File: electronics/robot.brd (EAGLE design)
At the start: 170.3 x 155.9 mm, 83 parts, among them J1 USB-B, J3 B6B-ZR, J4 B6B-ZR, J5 B6B-ZR, J6 KICKER, Q1 IRLMS2002TRPBF, Q2 IRLMS2002TRPBF, Q3 NPN_BC817,215, Q4 SUD50N04-8M8P-4GE3, Q5 NPN_BC817,215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

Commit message: Electronic fixes
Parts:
- removed S1: DPDT, rhoban:L202021MA04Q
- added C17: 1µF, SparkFun-Capacitors:0805
- added Q7: IRLMS2002TRPBF, rhoban:SOT23-6
- added R18: 56K, SparkFun-Resistors:0805
- added U$1: L102011ML04Q, rhoban:L102011ML04Q
- moved J2 24.0 mm to (30.5, 7.39)
- moved Q1 8.75 mm to (22.4, 23.6)
- moved Q2 8.75 mm to (18.7, 23.6)
- moved R3 8.75 mm to (20.7, 17.1)
- moved R5 8.75 mm to (17.0, 17.1)
- moved U3 8.75 mm to (26.1, 23.6)
- moved C7 8.75 mm to (21.1, 27.9)
- moved C8 8.75 mm to (23.4, 27.8)
- moved R10 8.75 mm to (15.6, 23.7)
- moved R11 8.75 mm to (24.4, 20.1)
- moved R7 8.75 mm to (25.9, 27.8)
- moved R9 8.75 mm to (17.7, 28.9)
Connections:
- new net N$19: C17.2, Q7.3, R18.2
- net GND_RAW: now also Q7.4, R18.1; no longer S1.P4
- net N$13: now also Q7.1, Q7.2, Q7.5, Q7.6; no longer S1.P5
- net N$7: now also U$1.P$2; no longer S1.P2
- net VIN: now also C17.1, U$1.P$1; no longer S1.P3

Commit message: Upgrading capacitors to 3300uF
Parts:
- C19, C20: value 2200uF -> 3300uF
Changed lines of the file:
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@@
 <attribute name="FARNELL" value="JF-0530B" x="-63.639453125" y="27.664428125" size="1.778" layer="27" font="vector" rot="R330" display="off"/>
 </element>
-<element name="C19" library="rcl" package="E5-13" value="2200uF" x="-46.560271875" y="45.22785625" rot="R240">
-<attribute name="FARNELL" value="2749341" x="-46.560271875" y="45.22785625" size="1.778" layer="27" rot="R240" display="off"/>
+<element name="C19" library="rcl" package="E5-13" value="3300uF" x="-46.560271875" y="45.22785625" rot="R240">
+<attribute name="MOUSER" value="710-860160278042 " x="-46.560271875" y="45.22785625" size="1.778" layer="27" rot="R240" display="off"/>
 </element>
-<element name="C20" library="rcl" package="E5-13" value="2200uF" x="-63.309496875" y="17.42513125" rot="R60">
-<attribute name="FARNELL" value="2749341" x="-63.309496875" y="17.42513125" size="1.778" layer="27" rot="R60" display="off"/>
+<element name="C20" library="rcl" package="E5-13" value="3300uF" x="-63.309496875" y="17.42513125" rot="R60">
+<attribute name="MOUSER" value="710-860160278042 " x="-63.309496875" y="17.42513125" size="1.778" layer="27" rot="R60" display="off"/>
 </element>
 <element name="C1" library="SparkFun-Capacitors" package="0805" value="0.1µF" x="-19.29488125" y="-38.44696875" rot="R300">

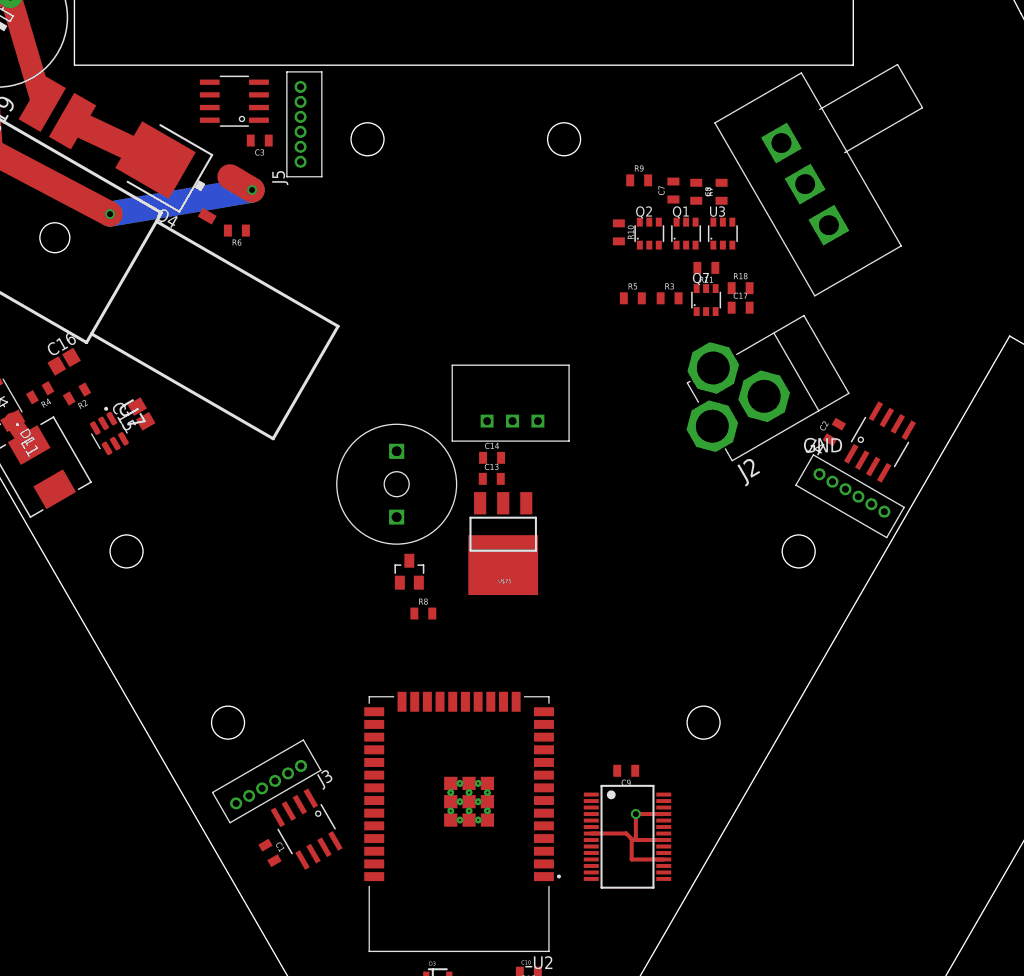
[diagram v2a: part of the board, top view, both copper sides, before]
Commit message: Preparing a switch to TOSHIBA H bridges
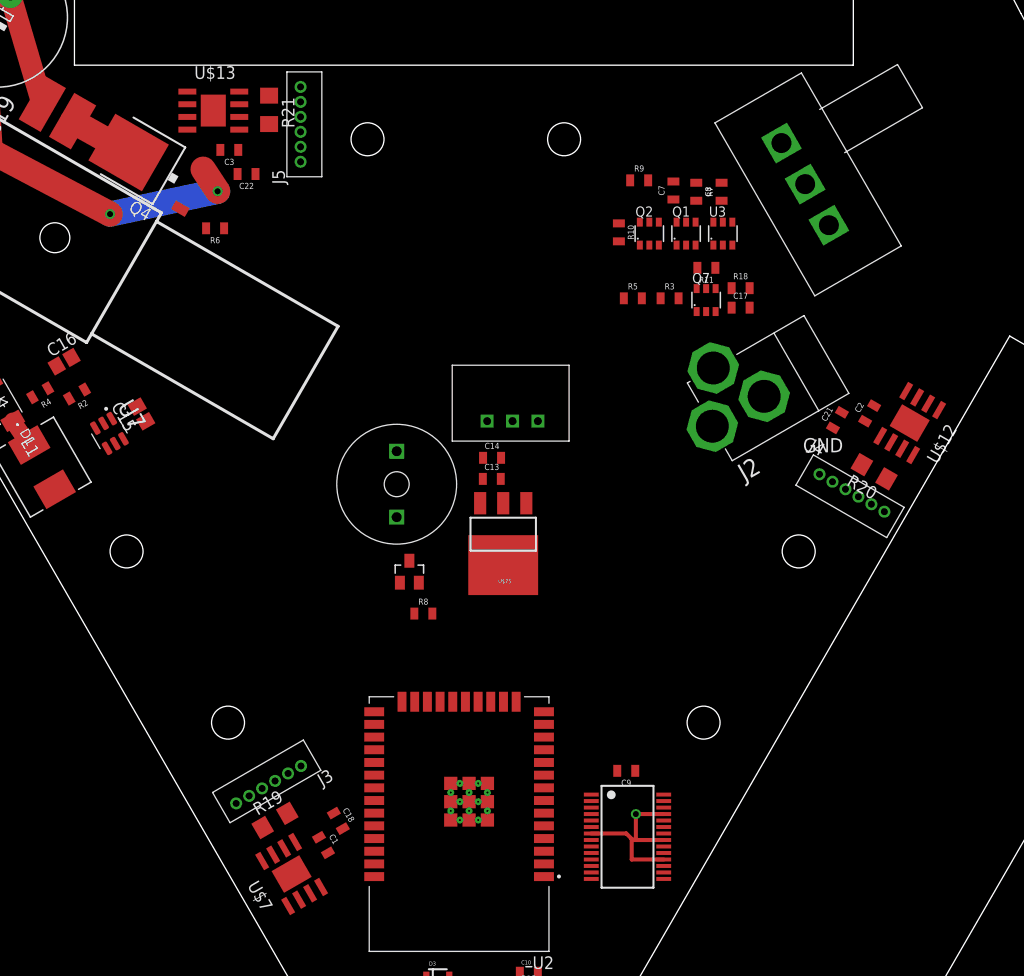
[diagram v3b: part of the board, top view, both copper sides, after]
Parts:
- removed U4, U5, U6: L9110, rhoban:SO8
- added C18, C21, C22: 1µF, SparkFun-Capacitors:0805
- added R19, R20, R21: 0.33, rcl:R1206
- added U$12, U$13, U$7: TB67H450FNG, rhoban:HSOP8
- moved C1 5.42 mm to (-13.9, -37.7)
- moved C2 3.99 mm to (40.8, 5.57)
- moved C3 3.19 mm to (-23.4, 32.0)
- moved Q4 2.80 mm to (-31.3, 30.4)
- moved R6 2.20 mm to (-24.8, 24.1)
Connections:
- new net N$18: R19.1, U$7.7
- new net N$20: R20.1, U$12.7
- new net N$21: R21.1, U$13.7
- net 3.3V: now also U$12.4, U$13.4, U$7.4
- net GND: now also C18.2, C21.2, C22.2, R19.2, R20.2, R21.2, U$12.1, U$13.1, U$7.1; no longer U4.5, U4.8, U5.5, U5.8, U6.5, U6.8
- net M1A: now also U$7.3; no longer U4.6
- net M1B: now also U$7.2; no longer U4.7
- net M1P1: now also U$7.6; no longer U4.1
- net M1P2: now also U$7.8; no longer U4.4
- net M2A: now also U$12.3; no longer U5.6
- net M2B: now also U$12.2; no longer U5.7
- net M2P1: now also U$12.6; no longer U5.1
- net M2P2: now also U$12.8; no longer U5.4
- net M3A: now also U$13.3; no longer U6.6
- net M3B: now also U$13.2; no longer U6.7
- net M3P1: now also U$13.6; no longer U6.1
- net M3P2: now also U$13.8; no longer U6.4
- net VIN: now also C18.1, C21.1, C22.1, U$12.5, U$13.5, U$7.5; no longer U4.2, U4.3, U5.2, U5.3, U6.2, U6.3
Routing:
- net GND: track 80.6 -> 77.3 mm
- net KICKER: track 9.18 -> 6.43 mm
